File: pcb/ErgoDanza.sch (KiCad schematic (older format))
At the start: 1 part, among them SW1 SW_Push

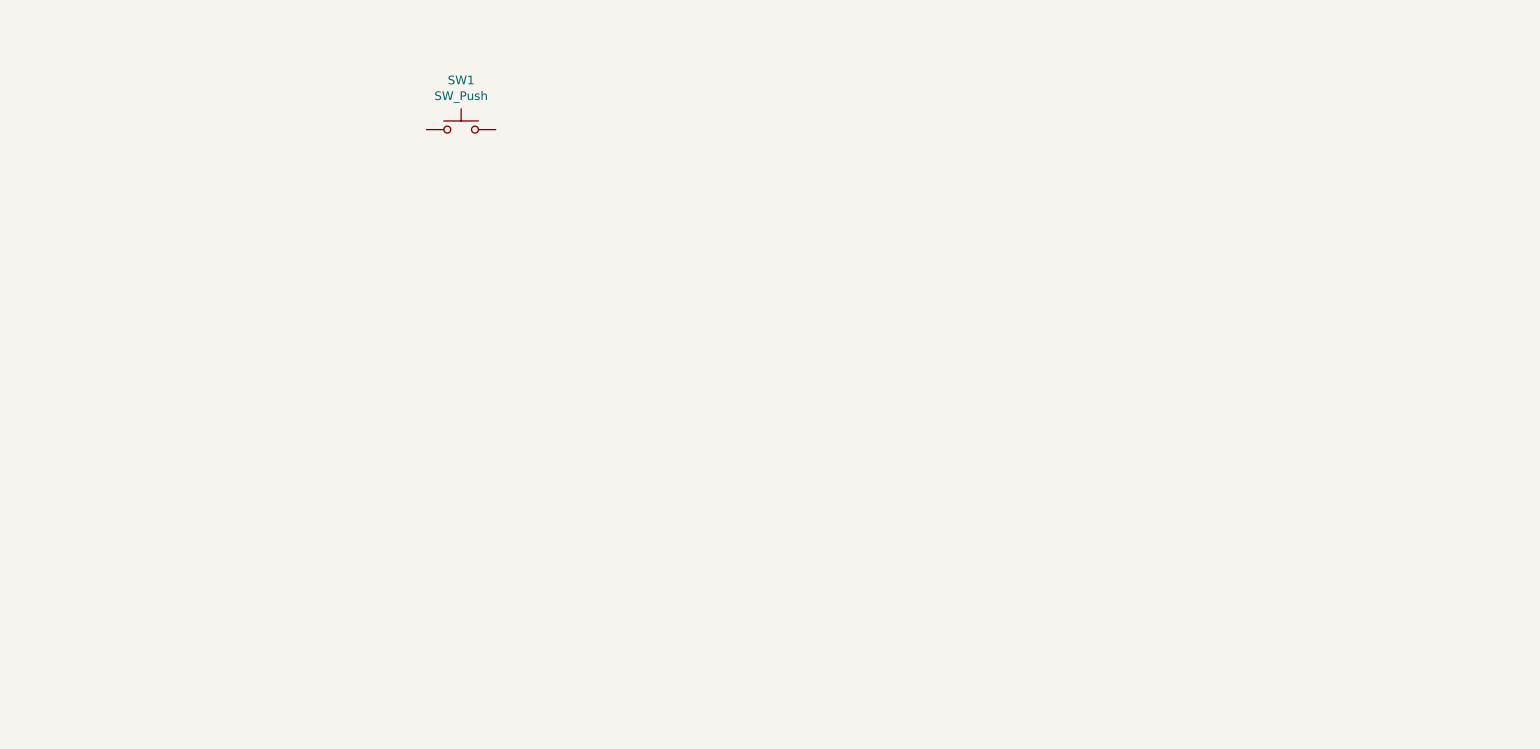
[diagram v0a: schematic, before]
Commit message: Initial adding of switches on one side.
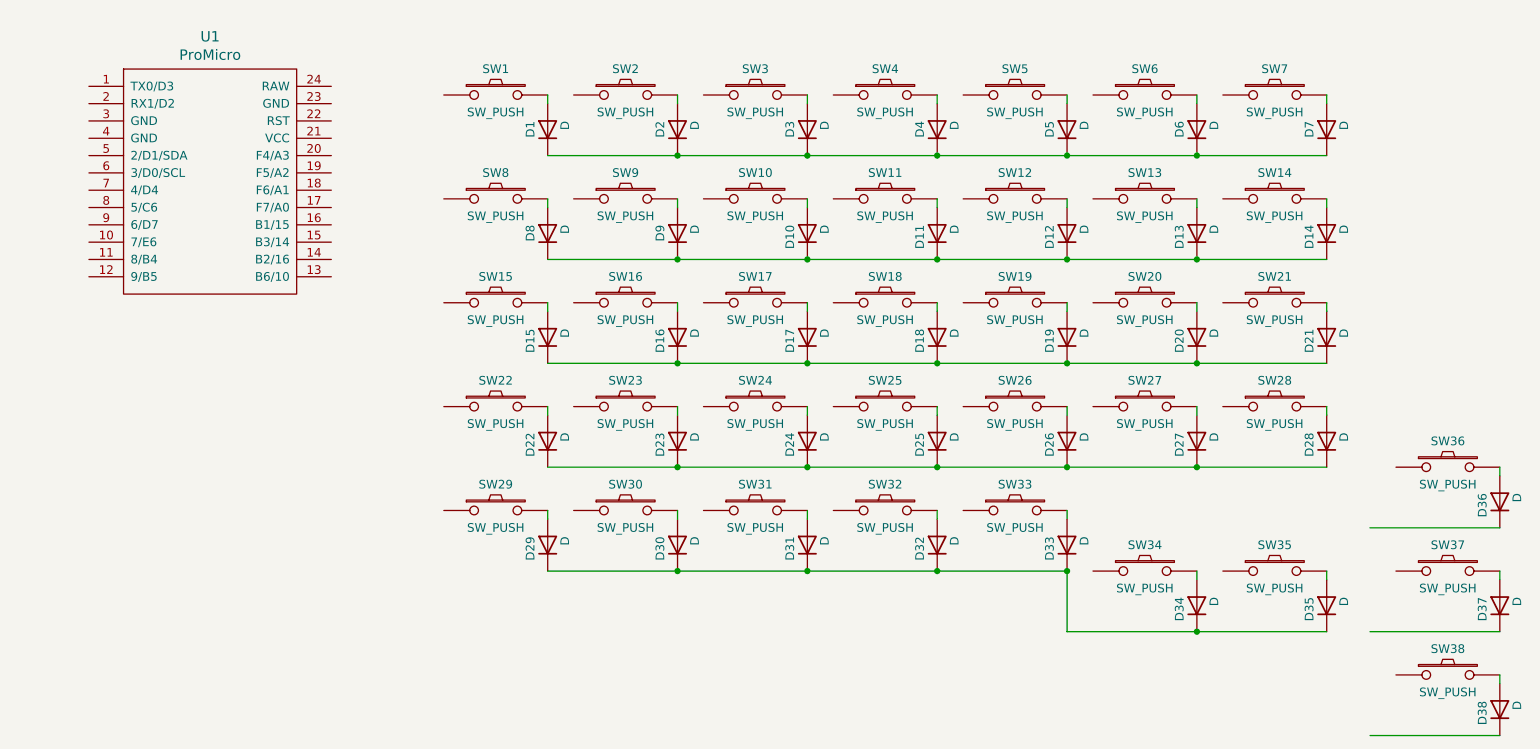
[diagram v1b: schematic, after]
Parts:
- removed SW1: SW_Push, symbol Switch:SW_Push
- added D1, D10, D11, D12, D13, D14, D15, D16, D17, D18, D19, D2, D20, D21, D22, D23, D24, D25, D26, D27, D28, D29, D3, D30, D31, D32, D33, D34, D35, D36, D37, D38, D4, D5, D6, D7, D8, D9: D, symbol Device:D
- added SW1, SW10, SW11, SW12, SW13, SW14, SW15, SW16, SW17, SW18, SW19, SW2, SW20, SW21, SW22, SW23, SW24, SW25, SW26, SW27, SW28, SW29, SW3, SW30, SW31, SW32, SW33, SW34, SW35, SW36, SW37, SW38, SW4, SW5, SW6, SW7, SW8, SW9: SW_PUSH, symbol kbd:SW_PUSH
- added U1: ProMicro, symbol kbd:ProMicro
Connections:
- wire segments 0 -> 72

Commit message: Connect all switches of left hand side.
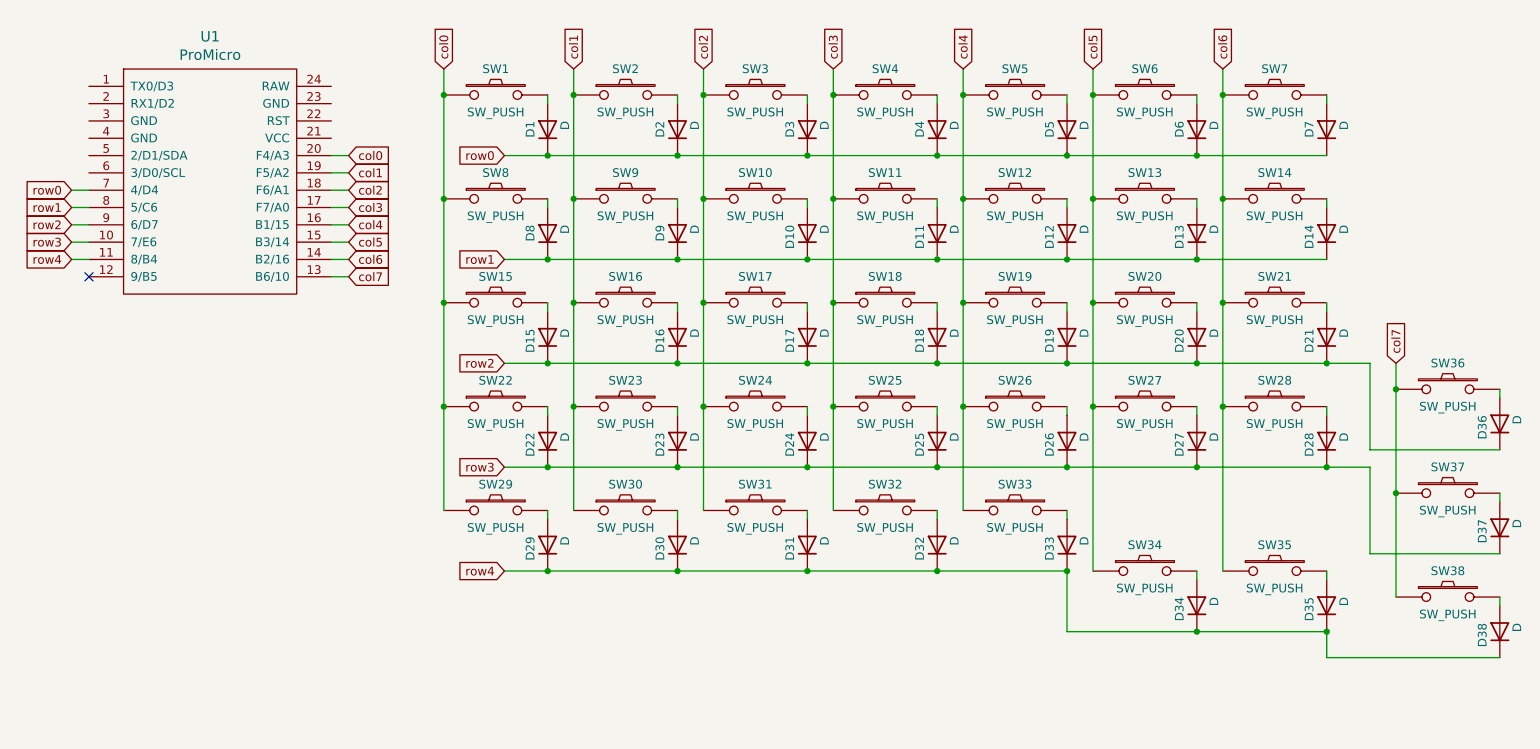
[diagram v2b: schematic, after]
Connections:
- net labels added: col0, col1, col2, col3, col4, col5, col6, col7, row0, row1, row2, row3, row4
- wire segments 72 -> 133
- no-connect marks 0 -> 1
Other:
- moved on the sheet: D36, D37, D38, SW36, SW37, SW38

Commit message: Power, Reset, Jack
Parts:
- added J1: MJ-4PP-9, symbol kbd:MJ-4PP-9
- added RSW1: SW_PUSH, symbol kbd:SW_PUSH
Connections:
- net data: now reaches U1.2 (RX1/D2)
- net data: now also J1.C
- net VCC: now reaches U1.21 (VCC)
- net VCC: now also J1.D
- net reset: now reaches U1.22 (RST)
- net reset: now also RSW1.1
- net GND: now reaches U1.23 (GND)
- net GND: now also U1.3 (GND), U1.4 (GND), J1.B, RSW1.2
- no-connect marks 1 -> 3
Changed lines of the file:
@@
 	8300 3150 8050 3150
 Connection ~ 8050 3150
+$Comp
+L power:GND #PWR?
+U 1 1 617E9DF2
+P 2600 1050
+F 0 "#PWR?" H 2600 800 50  0001 C CNN
+F 1 "GND" H 2700 900 50  0000 R CNN
+F 2 "" H 2600 1050 50  0001 C CNN
+F 3 "" H 2600 1050 50  0001 C CNN
+	1    2600 1050
+	0    -1   -1   0
+$EndComp
+Wire Wire Line
+	2600 1050 2300 1050
+$Comp
+L power:VCC #PWR?
+U 1 1 61802A34
+P 2600 1250
+F 0 "#PWR?" H 2600 1100 50  0001 C CNN
+F 1 "VCC" H 2500 1400 50  0000 L CNN
+F 2 "" H 2600 1250 50  0001 C CNN
+F 3 "" H 2600 1250 50  0001 C CNN
+	1    2600 1250
+	0    1    1    0
+$EndComp
+Wire Wire Line
+	2600 1250 2300 1250
+$Comp
+L power:GND #PWR?
+U 1 1 6180F816
+P 700 1250
+F 0 "#PWR?" H 700 1000 50  0001 C CNN
+F 1 "GND" H 750 1100 50  0000 R CNN
+F 2 "" H 700 1250 50  0001 C CNN
+F 3 "" H 700 1250 50  0001 C CNN
+	1    700  1250
+	0    1    1    0
+$EndComp
+Wire Wire Line
+	700  1250 750  1250
+Wire Wire Line
+	900  1150 750  1150
+Wire Wire Line
+	750  1150 750  1250
+Connection ~ 750  1250
+Wire Wire Line
+	750  1250 900  1250
+$Comp
+L power:PWR_FLAG #FLG?
+U 1 1 6181D087
+P 2150 2550
+F 0 "#FLG?" H 2150 2625 50  0001 C CNN
+F 1 "PWR_FLAG" H 2150 2723 50  0000 C CNN
+F 2 "" H 2150 2550 50  0001 C CNN
+F 3 "~" H 2150 2550 50  0001 C CNN
+	1    2150 2550
+	1    0    0    -1
+$EndComp
+$Comp
+L power:PWR_FLAG #FLG?
+U 1 1 6181D899
+P 2500 2700
+F 0 "#FLG?" H 2500 2775 50  0001 C CNN
+F 1 "PWR_FLAG" H 2500 2873 50  0000 C CNN
+F 2 "" H 2500 2700 50  0001 C CNN
+F 3 "~" H 2500 2700 50  0001 C CNN
+	1    2500 2700
+	-1   0    0    1
+$EndComp
+$Comp
+L power:GND #PWR?
+U 1 1 61820C59
+P 2150 2700
+F 0 "#PWR?" H 2150 2450 50  0001 C CNN
+F 1 "GND" H 2155 2527 50  0000 C CNN
+F 2 "" H 2150 2700 50  0001 C CNN
+F 3 "" H 2150 2700 50  0001 C CNN
+	1    2150 2700
+	1    0    0    -1
+$EndComp
+$Comp
+L power:VCC #PWR?
+U 1 1 61821436
+P 2500 2550
+F 0 "#PWR?" H 2500 2400 50  0001 C CNN
+F 1 "VCC" H 2515 2723 50  0000 C CNN
+F 2 "" H 2500 2550 50  0001 C CNN
+F 3 "" H 2500 2550 50  0001 C CNN
+	1    2500 2550
+	1    0    0    -1
+$EndComp
+Wire Wire Line
+	2500 2550 2500 2700
+Wire Wire Line
+	2150 2700 2150 2550
+$Comp
+L kbd:SW_PUSH RSW1
+U 1 1 6183CD28
+P 1350 2650
+F 0 "RSW1" H 1350 2800 50  0000 C CNN
+F 1 "SW_PUSH" H 1350 2550 50  0000 C CNN
+F 2 "" H 1350 2650 50  0000 C CNN
+F 3 "" H 1350 2650 50  0000 C CNN
+	1    1350 2650
+	1    0    0    -1
+$EndComp
+Text GLabel 1000 2650 0    50   Input ~ 0
+reset
+Text GLabel 2400 1150 2    50   Input ~ 0
+reset
+Wire Wire Line
+	2400 1150 2300 1150
+NoConn ~ 2300 950
+Wire Wire Line
+	1000 2650 1050 2650
+$Comp
+L power:GND #PWR?
+U 1 1 6189BC2A
+P 1750 2700
+F 0 "#PWR?" H 1750 2450 50  0001 C CNN
+F 1 "GND" H 1800 2550 50  0000 R CNN
+F 2 "" H 1750 2700 50  0001 C CNN
+F 3 "" H 1750 2700 50  0001 C CNN
+	1    1750 2700
+	1    0    0    -1
+$EndComp
+Wire Wire Line
+	1750 2650 1650 2650
+Wire Wire Line
+	1750 2700 1750 2650
+$Comp
+L kbd:MJ-4PP-9 J1
+U 1 1 618C2073
+P 1350 3400
+F 0 "J1" H 1350 3550 50  0000 C CNN
+F 1 "MJ-4PP-9" H 1350 3250 50  0000 C CNN
+F 2 "" H 1625 3575 50  0001 C CNN
+F 3 "~" H 1625 3575 50  0001 C CNN
+	1    1350 3400
+	1    0    0    -1
+$EndComp
+$Comp
+L power:VCC #PWR?
+U 1 1 618D4CD4
+P 1700 3300
+F 0 "#PWR?" H 1700 3150 50  0001 C CNN
+F 1 "VCC" H 1715 3473 50  0000 C CNN
+F 2 "" H 1700 3300 50  0001 C CNN
+F 3 "" H 1700 3300 50  0001 C CNN
+	1    1700 3300
+	1    0    0    -1
+$EndComp
+NoConn ~ 1550 3325
+Wire Wire Line
+	1700 3300 1700 3375
+Wire Wire Line
+	1700 3375 1550 3375
+$Comp
+L power:GND #PWR?
+U 1 1 618F5DB2
+P 1700 3550
+F 0 "#PWR?" H 1700 3300 50  0001 C CNN
+F 1 "GND" H 1705 3377 50  0000 C CNN
+F 2 "" H 1700 3550 50  0001 C CNN
+F 3 "" H 1700 3550 50  0001 C CNN
+	1    1700 3550
+	1    0    0    -1
+$EndComp
+Wire Wire Line
+	1700 3550 1700 3475
+Wire Wire Line
+	1700 3475 1550 3475
+Text GLabel 1725 3425 2    50   Input ~ 0
+data
+Wire Wire Line
+	1725 3425 1550 3425
+Text GLabel 800  1050 0    50   Input ~ 0
+data
+Wire Wire Line
+	800  1050 900  1050
 $EndSCHEMATC
